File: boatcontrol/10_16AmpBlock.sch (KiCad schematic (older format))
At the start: 13 parts, among them U6101 ULN2803A

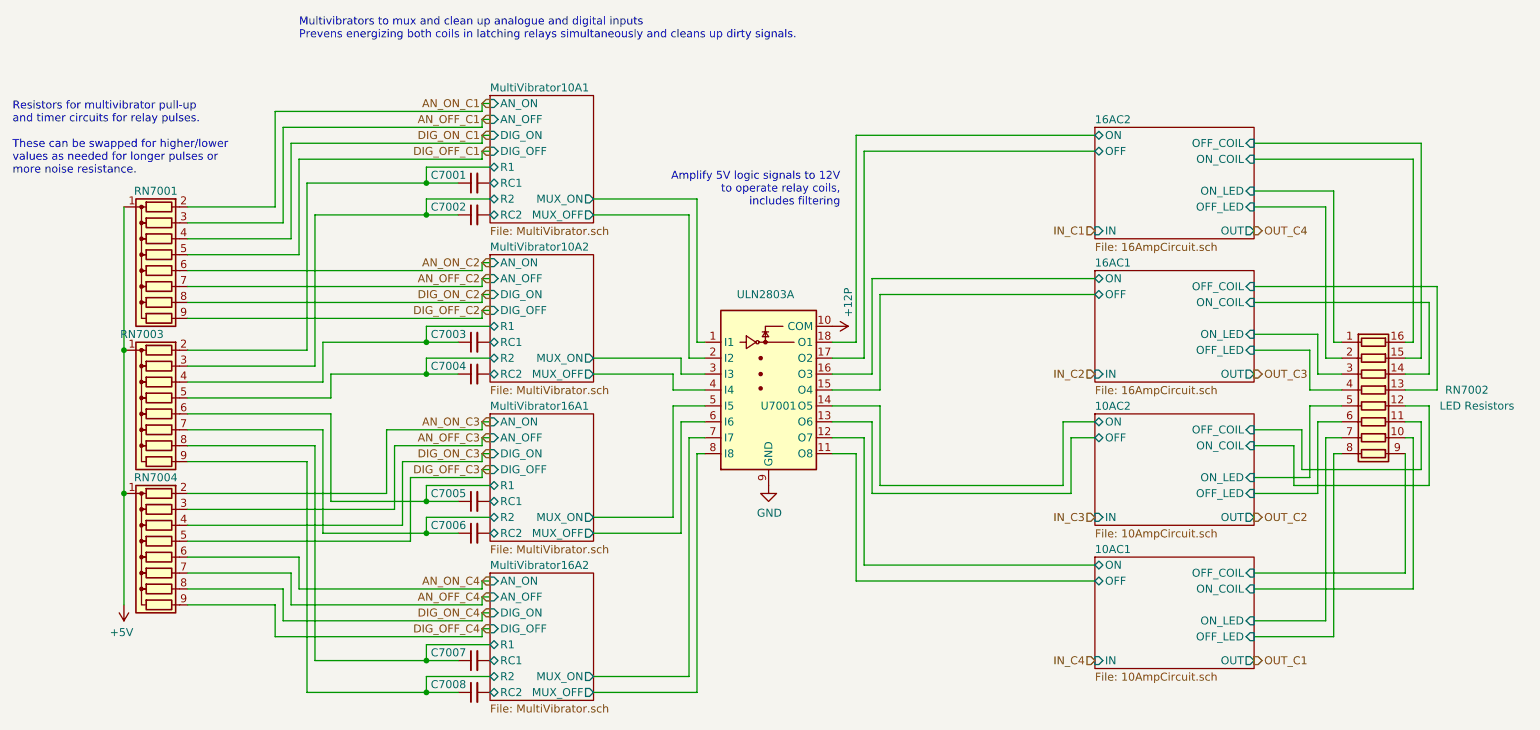
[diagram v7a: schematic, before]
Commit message: Add remaining bypass capacitors
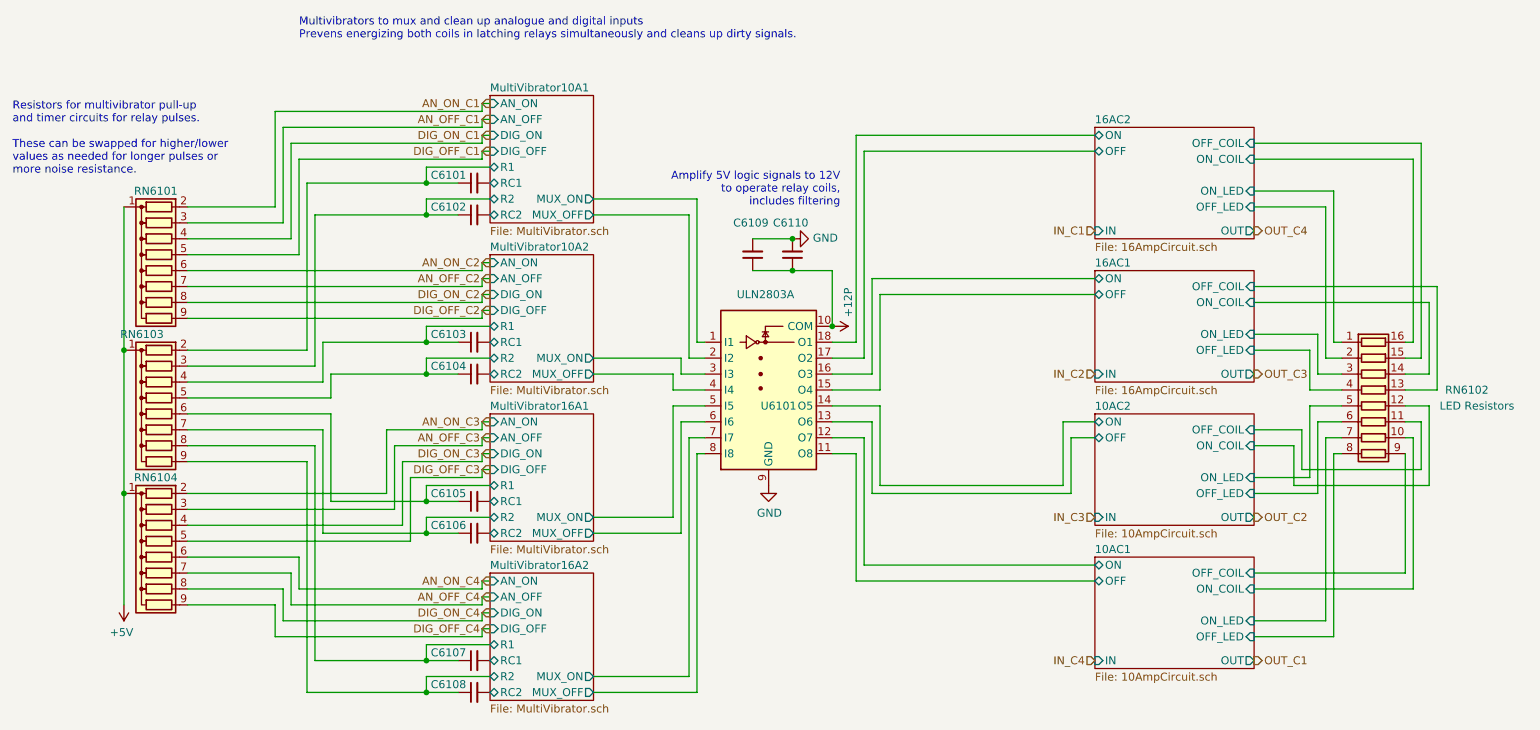
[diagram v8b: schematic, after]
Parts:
- added C6109: 10uF, Capacitor_THT:C_Disc_D7.5mm_W5.0mm_P5.00mm, symbol Device:C_Small
- added C6110: 0.1uF, Capacitor_THT:C_Disc_D7.5mm_W5.0mm_P5.00mm, symbol Device:C_Small
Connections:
- net +12P: now also C6109.1, C6110.1
- net GND: now also C6109.2, C6110.2
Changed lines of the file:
@@
 $Descr A4 11693 8268
 encoding utf-8
-Sheet 70 87
+Sheet 61 87
 Title "Boat Control Hat"
 Date "2020-07-09"
@@
 AR Path="/D1BB8DB4/5F76AF55/604747A2" Ref="#PWR06101"  Part="1"
 AR Path="/D1BB8DB4/5F75E923/604747A2" Ref="#PWR07001"  Part="1"
-F 0 "#PWR07001" H 6900 3250 50  0001 C CNN
+F 0 "#PWR06101" H 6900 3250 50  0001 C CNN
 F 1 "+12P" H 6750 3500 50  0000 C CNN
 F 2 "" H 6900 3400 50  0001 C CNN
@@
 AR Path="/D1BB8DB4/5F76AF55/604747AF" Ref="U6101"  Part="1"
 AR Path="/D1BB8DB4/5F75E923/604747AF" Ref="U7001"  Part="1"
-F 0 "U7001" H 6450 3500 50  0000 L CNN
+F 0 "U6101" H 6450 3500 50  0000 L CNN
 F 1 "ULN2803A" H 6300 4200 50  0000 L CNN
 F 2 "Package_DIP:DIP-18_W7.62mm" H 6550 3050 50  0001 L CNN
@@
 AR Path="/D1BB8DB4/5F76AF55/604747C1" Ref="#PWR06102"  Part="1"
 AR Path="/D1BB8DB4/5F75E923/604747C1" Ref="#PWR07002"  Part="1"
-F 0 "#PWR07002" H 6500 4150 50  0001 C CNN
+F 0 "#PWR06102" H 6500 4150 50  0001 C CNN
 F 1 "GND" H 6505 4227 50  0000 C CNN
 F 2 "" H 6500 4400 50  0001 C CNN
@@
 AR Path="/D1BB8DB4/5F76AF55/6047484A" Ref="#PWR06103"  Part="1"
 AR Path="/D1BB8DB4/5F75E923/6047484A" Ref="#PWR07003"  Part="1"
-F 0 "#PWR07003" H 2450 5000 50  0001 C CNN
+F 0 "#PWR06103" H 2450 5000 50  0001 C CNN
 F 1 "+5V" H 2465 5323 50  0000 C CNN
 F 2 "" H 2450 5150 50  0001 C CNN
@@
 AR Path="/D1BB8DB4/5F76AF55/60474926" Ref="RN6102"  Part="1"
 AR Path="/D1BB8DB4/5F75E923/60474926" Ref="RN7002"  Part="1"
-F 0 "RN7002" V 10200 4350 50  0000 L CNN
+F 0 "RN6102" V 10200 4350 50  0000 L CNN
 F 1 "680Ω" V 9800 3750 50  0001 L CNN
 F 2 "BoatControl:DIP254P762X432-16P" V 10775 3900 50  0001 C CNN
@@
 AR Path="/D1BB8DB4/5F75E923/62B5C7B5" Ref="C7001"  Part="1"
 AR Path="/D1BB8DB4/5F76AF55/62B5C7B5" Ref="C6101"  Part="1"
-F 0 "C7001" V 4600 2550 50  0000 L CNN
+F 0 "C6101" V 4600 2550 50  0000 L CNN
 F 1 "1µF" H 3800 2400 50  0001 L CNN
 F 2 "Capacitor_THT:C_Disc_D7.5mm_W5.0mm_P5.00mm" H 4650 2500 50  0001 C CNN
@@
 AR Path="/D1BB8DB4/5F75E923/62B76848" Ref="C7002"  Part="1"
 AR Path="/D1BB8DB4/5F76AF55/62B76848" Ref="C6102"  Part="1"
-F 0 "C7002" V 4600 2750 50  0000 L CNN
+F 0 "C6102" V 4600 2750 50  0000 L CNN
 F 1 "1µF" H 3800 2600 50  0001 L CNN
 F 2 "Capacitor_THT:C_Disc_D7.5mm_W5.0mm_P5.00mm" H 4650 2700 50  0001 C CNN
@@
 AR Path="/D1BB8DB4/5F75E923/62B86A50" Ref="C7003"  Part="1"
 AR Path="/D1BB8DB4/5F76AF55/62B86A50" Ref="C6103"  Part="1"
-F 0 "C7003" V 4600 3550 50  0000 L CNN
+F 0 "C6103" V 4600 3550 50  0000 L CNN
 F 1 "1µF" H 3800 3400 50  0001 L CNN
 F 2 "Capacitor_THT:C_Disc_D7.5mm_W5.0mm_P5.00mm" H 4650 3500 50  0001 C CNN
@@
 AR Path="/D1BB8DB4/5F75E923/62B939DB" Ref="C7004"  Part="1"
 AR Path="/D1BB8DB4/5F76AF55/62B939DB" Ref="C6104"  Part="1"
-F 0 "C7004" V 4600 3750 50  0000 L CNN
+F 0 "C6104" V 4600 3750 50  0000 L CNN
 F 1 "1µF" H 3800 3600 50  0001 L CNN
 F 2 "Capacitor_THT:C_Disc_D7.5mm_W5.0mm_P5.00mm" H 4650 3700 50  0001 C CNN
@@
 AR Path="/D1BB8DB4/5F75E923/62BA14CE" Ref="C7005"  Part="1"
 AR Path="/D1BB8DB4/5F76AF55/62BA14CE" Ref="C6105"  Part="1"
-F 0 "C7005" V 4600 4550 50  0000 L CNN
+F 0 "C6105" V 4600 4550 50  0000 L CNN
 F 1 "1µF" H 3800 4400 50  0001 L CNN
 F 2 "Capacitor_THT:C_Disc_D7.5mm_W5.0mm_P5.00mm" H 4650 4500 50  0001 C CNN
@@
 AR Path="/D1BB8DB4/5F75E923/62BAE342" Ref="C7006"  Part="1"
 AR Path="/D1BB8DB4/5F76AF55/62BAE342" Ref="C6106"  Part="1"
-F 0 "C7006" V 4600 4750 50  0000 L CNN
+F 0 "C6106" V 4600 4750 50  0000 L CNN
 F 1 "1µF" H 3800 4600 50  0001 L CNN
 F 2 "Capacitor_THT:C_Disc_D7.5mm_W5.0mm_P5.00mm" H 4650 4700 50  0001 C CNN
@@
 AR Path="/D1BB8DB4/5F75E923/62BBBC28" Ref="C7007"  Part="1"
 AR Path="/D1BB8DB4/5F76AF55/62BBBC28" Ref="C6107"  Part="1"
-F 0 "C7007" V 4600 5550 50  0000 L CNN
+F 0 "C6107" V 4600 5550 50  0000 L CNN
 F 1 "1µF" H 3800 5400 50  0001 L CNN
 F 2 "Capacitor_THT:C_Disc_D7.5mm_W5.0mm_P5.00mm" H 4650 5500 50  0001 C CNN
@@
 AR Path="/D1BB8DB4/5F75E923/62BC8A92" Ref="C7008"  Part="1"
 AR Path="/D1BB8DB4/5F76AF55/62BC8A92" Ref="C6108"  Part="1"
-F 0 "C7008" V 4600 5750 50  0000 L CNN
+F 0 "C6108" V 4600 5750 50  0000 L CNN
 F 1 "1µF" H 3800 5600 50  0001 L CNN
 F 2 "Capacitor_THT:C_Disc_D7.5mm_W5.0mm_P5.00mm" H 4650 5700 50  0001 C CNN
@@
 AR Path="/D1BB8DB4/5F75E923/62CB5764" Ref="RN7003"  Part="1"
 AR Path="/D1BB8DB4/5F76AF55/62CB5764" Ref="RN6103"  Part="1"
-F 0 "RN7003" V 2150 3900 50  0000 L CNN
+F 0 "RN6103" V 2150 3900 50  0000 L CNN
 F 1 "10MΩ" H 2300 3550 50  0001 L CNN
 F 2 "Resistor_THT:R_Array_SIP9" V 3125 3950 50  0001 C CNN
@@
 AR Path="/D1BB8DB4/5F76AF55/630078FE" Ref="RN6101"  Part="1"
 AR Path="/D1BB8DB4/5F75E923/630078FE" Ref="RN7001"  Part="1"
-F 0 "RN7001" V 2150 3050 50  0000 C CNN
+F 0 "RN6101" V 2150 3050 50  0000 C CNN
 F 1 "100KΩ" V 2450 2750 50  0001 C CNN
 F 2 "Resistor_THT:R_Array_SIP9" H 3400 3150 50  0001 L CNN
@@
 AR Path="/D1BB8DB4/5F76AF55/63015012" Ref="RN6104"  Part="1"
 AR Path="/D1BB8DB4/5F75E923/63015012" Ref="RN7004"  Part="1"
-F 0 "RN7004" V 2150 4850 50  0000 C CNN
+F 0 "RN6104" V 2150 4850 50  0000 C CNN
 F 1 "100KΩ" V 2450 4550 50  0001 C CNN
 F 2 "Resistor_THT:R_Array_SIP9" H 3400 4950 50  0001 L CNN
@@
 F9 "OFF_COIL" I R 9550 4050 50
 $EndSheet
+$Comp
+L Device:C_Small C?
+U 1 1 62505F9A
+P 6400 2950
+AR Path="/62505F9A" Ref="C?"  Part="1"
+AR Path="/D1BB8DB4/5F76AF55/62505F9A" Ref="C6109"  Part="1"
+AR Path="/D1BB8DB4/5F75E923/62505F9A" Ref="C7009"  Part="1"
+F 0 "C6109" H 6300 2750 50  0000 L CNN
+F 1 "10uF" H 6491 2905 50  0001 L CNN
+F 2 "Capacitor_THT:C_Disc_D7.5mm_W5.0mm_P5.00mm" H 6400 2950 50  0001 C CNN
+F 3 "https://www.mouser.ca/datasheet/2/212/KEM_C1050_GOLDMAX_X7R-1518817.pdf" H 6400 2950 50  0001 C CNN
+F 4 "Kemet" H 6400 2950 50  0001 C CNN "Manufacturer"
+F 5 "C322C106K3R5TA" V 6400 2950 50  0001 C CNN "Model"
+	1    6400 2950
+	-1   0    0    1
+$EndComp
+$Comp
+L Device:C_Small C?
+U 1 1 62505FA2
+P 6650 2950
+AR Path="/62505FA2" Ref="C?"  Part="1"
+AR Path="/D1BB8DB4/5F76AF55/62505FA2" Ref="C6110"  Part="1"
+AR Path="/D1BB8DB4/5F75E923/62505FA2" Ref="C7010"  Part="1"
+F 0 "C6110" H 6550 2750 50  0000 L CNN
+F 1 "0.1uF" H 6741 2905 50  0001 L CNN
+F 2 "Capacitor_THT:C_Disc_D7.5mm_W5.0mm_P5.00mm" H 6650 2950 50  0001 C CNN
+F 3 "https://www.mouser.ca/datasheet/2/212/KEM_C1050_GOLDMAX_X7R-1518817.pdf" H 6650 2950 50  0001 C CNN
+F 4 "Kemet" H 6650 2950 50  0001 C CNN "Manufacturer"
+F 5 "C320C104K3R5TA" V 6650 2950 50  0001 C CNN "Model"
+	1    6650 2950
+	-1   0    0    1
+$EndComp
+Wire Wire Line
+	6400 2850 6650 2850
+$Comp
+L power:GND #PWR?
+U 1 1 62505FA9
+P 6650 2850
+AR Path="/62505FA9" Ref="#PWR?"  Part="1"
+AR Path="/D1BB8DB4/5F75E923/62505FA9" Ref="#PWR0200"  Part="1"
+AR Path="/D1BB8DB4/5F76AF55/62505FA9" Ref="#PWR0199"  Part="1"
+F 0 "#PWR0199" H 6650 2600 50  0001 C CNN
+F 1 "GND" V 6655 2722 50  0000 R CNN
+F 2 "" H 6650 2850 50  0001 C CNN
+F 3 "" H 6650 2850 50  0001 C CNN
+	1    6650 2850
+	0    -1   -1   0
+$EndComp
+Connection ~ 6650 2850
+Wire Wire Line
+	6400 3050 6650 3050
+Wire Wire Line
+	6650 3050 6900 3050
+Wire Wire Line
+	6900 3050 6900 3400
+Connection ~ 6650 3050
+Connection ~ 6900 3400
 $EndSCHEMATC
